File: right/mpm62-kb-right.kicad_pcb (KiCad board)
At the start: 2 copper layers, 161.9 x 95.2 mm, 72 parts, among them J1 Conn_01x04_Male, SW1 SW_Push, U1 MCP23018-E_SP

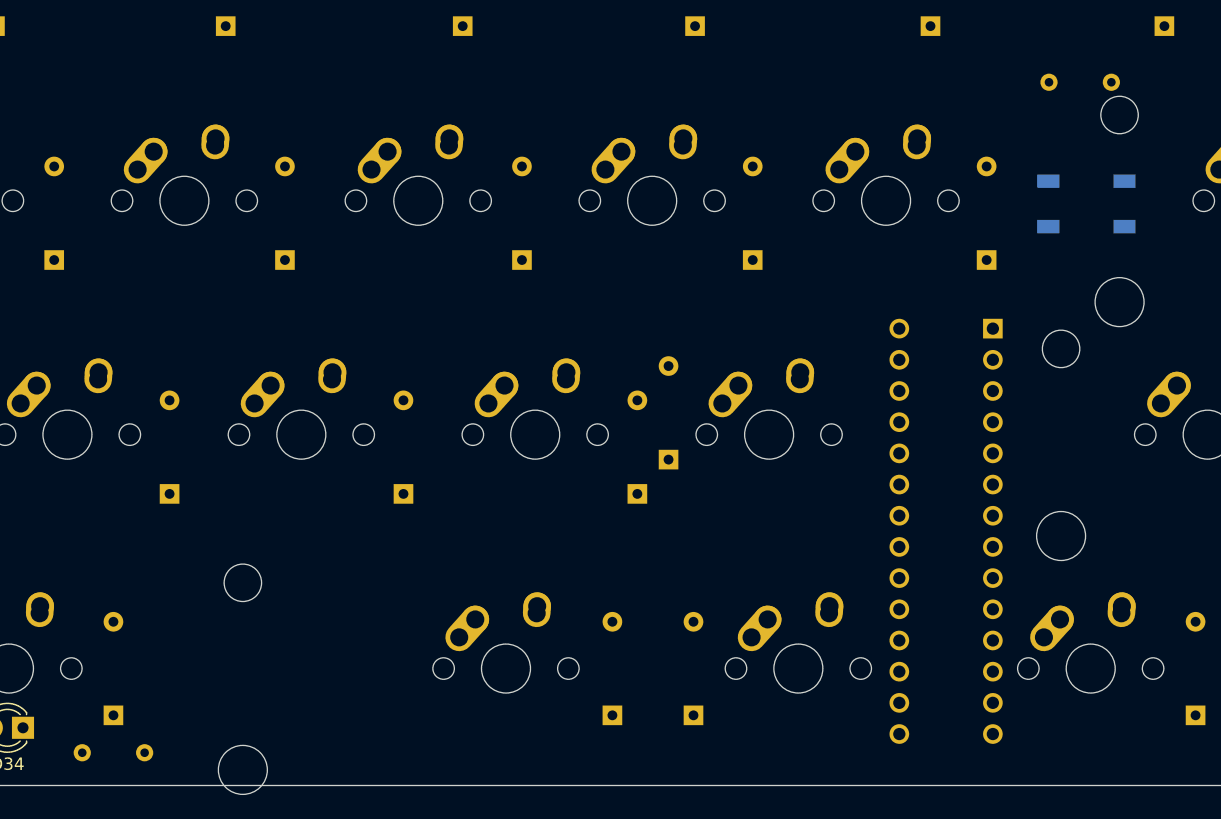
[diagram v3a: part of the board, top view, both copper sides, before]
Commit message: Fix resistor footprint, clean up layout.
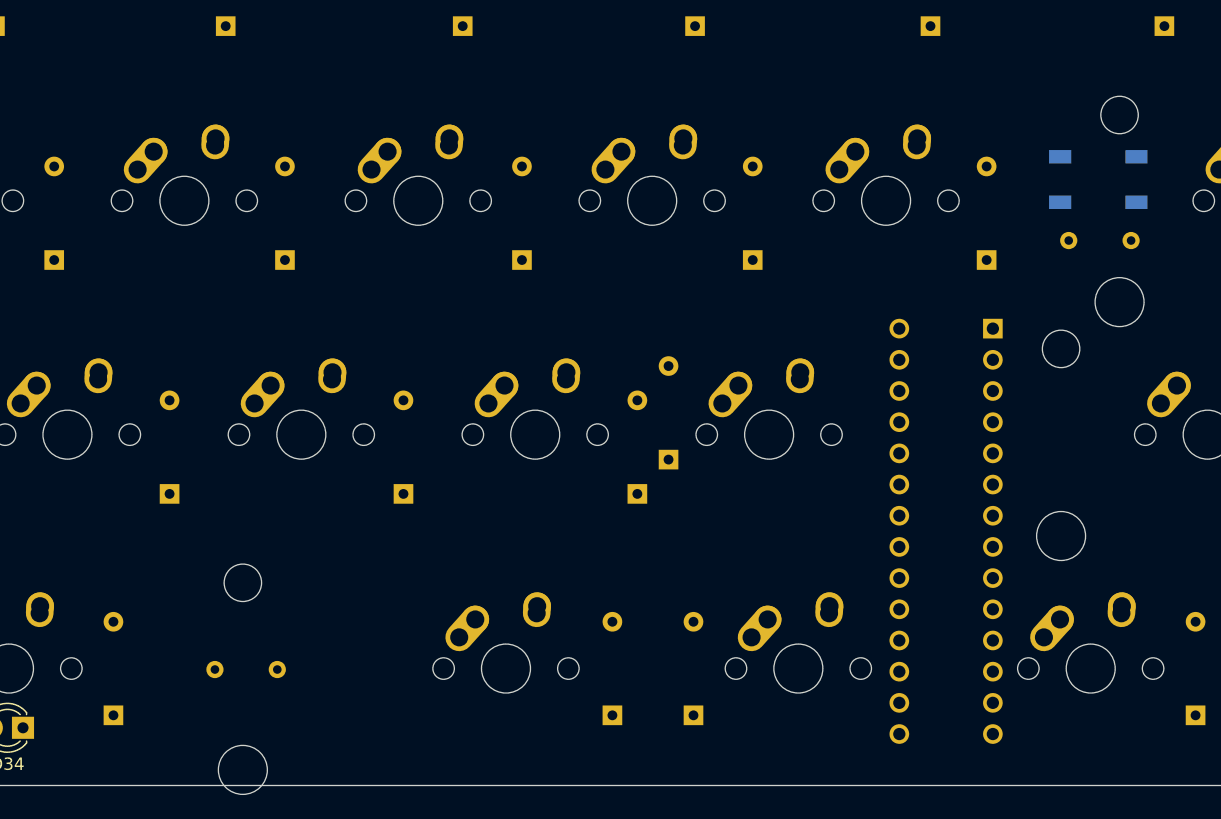
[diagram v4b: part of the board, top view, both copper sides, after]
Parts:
- R1, R2: footprint Resistor_THT:R_Axial_DIN0204_L3.6mm_D1.6mm_P5.08mm_Vertical -> Resistor_THT:R_Axial_DIN0204_L3.6mm_D1.6mm_P5.08mm_Horizontal
- moved R2 13.0 mm to (172.0, 98.5)
- moved R1 12.8 mm to (107.6, 133.4)
- moved SW1 2.21 mm to (174.4, 93.5), turned to 180 degrees
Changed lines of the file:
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@@
     (add_net VCC)
+  )
+  (module Resistor_THT:R_Axial_DIN0204_L3.6mm_D1.6mm_P5.08mm_Horizontal (layer B.Cu)
+    (at 172.04 98.49)
+    (descr "Resistor, Axial_DIN0204 series, Axial, Horizontal, pin pitch=5.08mm, 0.167W, length*diameter=3.6*1.6mm^2, http://cdn-reichelt.de/documents/datenblatt/B400/1_4W%23YAG.pdf")
+    (tags "Resistor Axial_DIN0204 series Axial Horizontal pin pitch 5.08mm 0.167W length 3.6mm diameter 1.6mm")
+    (fp_text reference R2 (at 2.54 1.92) (layer B.SilkS)
+      (effects (font (size 1 1) (thickness 0.15)) (justify mirror))
+    )
+    (fp_text value R_Small (at 2.54 -1.92) (layer B.Fab)
+      (effects (font (size 1 1) (thickness 0.15)) (justify mirror))
+    )
+    (fp_text user %R (at 2.54 0) (layer B.Fab)
+      (effects (font (size 0.72 0.72) (thickness 0.108)) (justify mirror))
+    )
+    (fp_line (start 6.03 1.05) (end -0.95 1.05) (layer B.CrtYd) (width 0.05))
+    (fp_line (start 6.03 -1.05) (end 6.03 1.05) (layer B.CrtYd) (width 0.05))
+    (fp_line (start -0.95 -1.05) (end 6.03 -1.05) (layer B.CrtYd) (width 0.05))
+    (fp_line (start -0.95 1.05) (end -0.95 -1.05) (layer B.CrtYd) (width 0.05))
+    (fp_line (start 0.62 -0.92) (end 4.46 -0.92) (layer B.SilkS) (width 0.12))
+    (fp_line (start 0.62 0.92) (end 4.46 0.92) (layer B.SilkS) (width 0.12))
+    (fp_line (start 5.08 0) (end 4.34 0) (layer B.Fab) (width 0.1))
+    (fp_line (start 0 0) (end 0.74 0) (layer B.Fab) (width 0.1))
+    (fp_line (start 4.34 0.8) (end 0.74 0.8) (layer B.Fab) (width 0.1))
+    (fp_line (start 4.34 -0.8) (end 4.34 0.8) (layer B.Fab) (width 0.1))
+    (fp_line (start 0.74 -0.8) (end 4.34 -0.8) (layer B.Fab) (width 0.1))
+    (fp_line (start 0.74 0.8) (end 0.74 -0.8) (layer B.Fab) (width 0.1))
+    (pad 2 thru_hole oval (at 5.08 0) (size 1.4 1.4) (drill 0.7) (layers *.Cu *.Mask)
+      (net 53 "Net-(R2-Pad2)"))
+    (pad 1 thru_hole circle (at 0 0) (size 1.4 1.4) (drill 0.7) (layers *.Cu *.Mask)
+      (net 41 VCC))
+    (model ${KISYS3DMOD}/Resistor_THT.3dshapes/R_Axial_DIN0204_L3.6mm_D1.6mm_P5.08mm_Horizontal.wrl
+      (at (xyz 0 0 0))
+      (scale (xyz 1 1 1))
+      (rotate (xyz 0 0 0))
+    )
+  )
+  (module Resistor_THT:R_Axial_DIN0204_L3.6mm_D1.6mm_P5.08mm_Horizontal (layer B.Cu)
+    (at 107.58 133.43 180)
+    (descr "Resistor, Axial_DIN0204 series, Axial, Horizontal, pin pitch=5.08mm, 0.167W, length*diameter=3.6*1.6mm^2, http://cdn-reichelt.de/documents/datenblatt/B400/1_4W%23YAG.pdf")
+    (tags "Resistor Axial_DIN0204 series Axial Horizontal pin pitch 5.08mm 0.167W length 3.6mm diameter 1.6mm")
+    (fp_text reference R1 (at 2.54 1.92) (layer B.SilkS)
+      (effects (font (size 1 1) (thickness 0.15)) (justify mirror))
+    )
+    (fp_text value R_Small (at 2.54 -1.92) (layer B.Fab)
+      (effects (font (size 1 1) (thickness 0.15)) (justify mirror))
+    )
+    (fp_text user %R (at 2.54 0) (layer B.Fab)
+      (effects (font (size 0.72 0.72) (thickness 0.108)) (justify mirror))
+    )
+    (fp_line (start 6.03 1.05) (end -0.95 1.05) (layer B.CrtYd) (width 0.05))
+    (fp_line (start 6.03 -1.05) (end 6.03 1.05) (layer B.CrtYd) (width 0.05))
+    (fp_line (start -0.95 -1.05) (end 6.03 -1.05) (layer B.CrtYd) (width 0.05))
+    (fp_line (start -0.95 1.05) (end -0.95 -1.05) (layer B.CrtYd) (width 0.05))
+    (fp_line (start 0.62 -0.92) (end 4.46 -0.92) (layer B.SilkS) (width 0.12))
+    (fp_line (start 0.62 0.92) (end 4.46 0.92) (layer B.SilkS) (width 0.12))
+    (fp_line (start 5.08 0) (end 4.34 0) (layer B.Fab) (width 0.1))
+    (fp_line (start 0 0) (end 0.74 0) (layer B.Fab) (width 0.1))
+    (fp_line (start 4.34 0.8) (end 0.74 0.8) (layer B.Fab) (width 0.1))
+    (fp_line (start 4.34 -0.8) (end 4.34 0.8) (layer B.Fab) (width 0.1))
+    (fp_line (start 0.74 -0.8) (end 4.34 -0.8) (layer B.Fab) (width 0.1))
+    (fp_line (start 0.74 0.8) (end 0.74 -0.8) (layer B.Fab) (width 0.1))
+    (pad 2 thru_hole oval (at 5.08 0 180) (size 1.4 1.4) (drill 0.7) (layers *.Cu *.Mask)
+      (net 40 "Net-(D34-Pad1)"))
+    (pad 1 thru_hole circle (at 0 0 180) (size 1.4 1.4) (drill 0.7) (layers *.Cu *.Mask)
+      (net 52 "Net-(R1-Pad1)"))
+    (model ${KISYS3DMOD}/Resistor_THT.3dshapes/R_Axial_DIN0204_L3.6mm_D1.6mm_P5.08mm_Horizontal.wrl
+      (at (xyz 0 0 0))
+      (scale (xyz 1 1 1))
+      (rotate (xyz 0 0 0))
+    )
   )
   (module MX_Alps_Hybrid:MX-3U-NoLED (layer F.Cu)
@@
     (pad 2 thru_hole oval (at 2.5 -4.5 86.0548) (size 2.831378 2.25) (drill 1.47 (offset 0.290689 0)) (layers *.Cu B.Mask)
       (net 17 "Net-(D11-Pad2)"))
-  )
-  (module Resistor_THT:R_Axial_DIN0204_L3.6mm_D1.6mm_P5.08mm_Vertical (layer B.Cu)
-    (at 170.434 85.598)
-    (descr "Resistor, Axial_DIN0204 series, Axial, Vertical, pin pitch=5.08mm, 0.167W, length*diameter=3.6*1.6mm^2, http://cdn-reichelt.de/documents/datenblatt/B400/1_4W%23YAG.pdf")
-    (tags "Resistor Axial_DIN0204 series Axial Vertical pin pitch 5.08mm 0.167W length 3.6mm diameter 1.6mm")
-    (fp_text reference R2 (at 2.54 1.92) (layer B.SilkS)
-      (effects (font (size 1 1) (thickness 0.15)) (justify mirror))
-    )
-    (fp_text value R_Small (at 2.54 -1.92) (layer B.Fab)
-      (effects (font (size 1 1) (thickness 0.15)) (justify mirror))
-    )
-    (fp_text user %R (at 2.54 1.92) (layer B.Fab)
-      (effects (font (size 1 1) (thickness 0.15)) (justify mirror))
-    )
-    (fp_line (start 6.03 1.05) (end -1.05 1.05) (layer B.CrtYd) (width 0.05))
-    (fp_line (start 6.03 -1.05) (end 6.03 1.05) (layer B.CrtYd) (width 0.05))
-    (fp_line (start -1.05 -1.05) (end 6.03 -1.05) (layer B.CrtYd) (width 0.05))
-    (fp_line (start -1.05 1.05) (end -1.05 -1.05) (layer B.CrtYd) (width 0.05))
-    (fp_line (start 0.92 0) (end 4.08 0) (layer B.SilkS) (width 0.12))
-    (fp_line (start 0 0) (end 5.08 0) (layer B.Fab) (width 0.1))
-    (fp_circle (center 0 0) (end 0.92 0) (layer B.SilkS) (width 0.12))
-    (fp_circle (center 0 0) (end 0.8 0) (layer B.Fab) (width 0.1))
-    (pad 2 thru_hole oval (at 5.08 0) (size 1.4 1.4) (drill 0.7) (layers *.Cu *.Mask)
-      (net 53 "Net-(R2-Pad2)"))
-    (pad 1 thru_hole circle (at 0 0) (size 1.4 1.4) (drill 0.7) (layers *.Cu *.Mask)
-      (net 41 VCC))
-    (model ${KISYS3DMOD}/Resistor_THT.3dshapes/R_Axial_DIN0204_L3.6mm_D1.6mm_P5.08mm_Vertical.wrl
-      (at (xyz 0 0 0))
-      (scale (xyz 1 1 1))
-      (rotate (xyz 0 0 0))
-    )
-  )
-  (module Resistor_THT:R_Axial_DIN0204_L3.6mm_D1.6mm_P5.08mm_Vertical (layer B.Cu)
-    (at 96.774 140.208 180)
-    (descr "Resistor, Axial_DIN0204 series, Axial, Vertical, pin pitch=5.08mm, 0.167W, length*diameter=3.6*1.6mm^2, http://cdn-reichelt.de/documents/datenblatt/B400/1_4W%23YAG.pdf")
-    (tags "Resistor Axial_DIN0204 series Axial Vertical pin pitch 5.08mm 0.167W length 3.6mm diameter 1.6mm")
-    (fp_text reference R1 (at 2.54 1.92) (layer B.SilkS)
-      (effects (font (size 1 1) (thickness 0.15)) (justify mirror))
-    )
-    (fp_text value R_Small (at 2.54 -1.92) (layer B.Fab)
-      (effects (font (size 1 1) (thickness 0.15)) (justify mirror))
-    )
-    (fp_text user %R (at 2.54 1.92) (layer B.Fab)
-      (effects (font (size 1 1) (thickness 0.15)) (justify mirror))
-    )
-    (fp_line (start 6.03 1.05) (end -1.05 1.05) (layer B.CrtYd) (width 0.05))
-    (fp_line (start 6.03 -1.05) (end 6.03 1.05) (layer B.CrtYd) (width 0.05))
-    (fp_line (start -1.05 -1.05) (end 6.03 -1.05) (layer B.CrtYd) (width 0.05))
-    (fp_line (start -1.05 1.05) (end -1.05 -1.05) (layer B.CrtYd) (width 0.05))
-    (fp_line (start 0.92 0) (end 4.08 0) (layer B.SilkS) (width 0.12))
-    (fp_line (start 0 0) (end 5.08 0) (layer B.Fab) (width 0.1))
-    (fp_circle (center 0 0) (end 0.92 0) (layer B.SilkS) (width 0.12))
-    (fp_circle (center 0 0) (end 0.8 0) (layer B.Fab) (width 0.1))
-    (pad 2 thru_hole oval (at 5.08 0 180) (size 1.4 1.4) (drill 0.7) (layers *.Cu *.Mask)
-      (net 40 "Net-(D34-Pad1)"))
-    (pad 1 thru_hole circle (at 0 0 180) (size 1.4 1.4) (drill 0.7) (layers *.Cu *.Mask)
-      (net 52 "Net-(R1-Pad1)"))
-    (model ${KISYS3DMOD}/Resistor_THT.3dshapes/R_Axial_DIN0204_L3.6mm_D1.6mm_P5.08mm_Vertical.wrl
-      (at (xyz 0 0 0))
-      (scale (xyz 1 1 1))
-      (rotate (xyz 0 0 0))
-    )
   )
   (module digikey-footprints:DIP-28_W7.62mm (layer B.Cu)
@@
   )
   (module random-keyboard-parts:SKQG-1155865 (layer B.Cu)
-    (at 173.482 95.504)
+    (at 174.45 93.52 180)
     (attr smd)
     (fp_text reference SW1 (at 0 -4.064) (layer B.SilkS)
@@
     (fp_line (start 2.6 -1.1) (end 1.1 -2.6) (layer B.Fab) (width 0.15))
     (fp_line (start -2.6 -1.1) (end -1.1 -2.6) (layer B.Fab) (width 0.15))
-    (pad 4 smd rect (at -3.1 -1.85) (size 1.8 1.1) (layers B.Cu B.Paste B.Mask))
-    (pad 3 smd rect (at 3.1 1.85) (size 1.8 1.1) (layers B.Cu B.Paste B.Mask))
-    (pad 2 smd rect (at -3.1 1.85) (size 1.8 1.1) (layers B.Cu B.Paste B.Mask)
+    (pad 4 smd rect (at -3.1 -1.85 180) (size 1.8 1.1) (layers B.Cu B.Paste B.Mask))
+    (pad 3 smd rect (at 3.1 1.85 180) (size 1.8 1.1) (layers B.Cu B.Paste B.Mask))
+    (pad 2 smd rect (at -3.1 1.85 180) (size 1.8 1.1) (layers B.Cu B.Paste B.Mask)
       (net 53 "Net-(R2-Pad2)"))
-    (pad 1 smd rect (at 3.1 -1.85) (size 1.8 1.1) (layers B.Cu B.Paste B.Mask)
+    (pad 1 smd rect (at 3.1 -1.85 180) (size 1.8 1.1) (layers B.Cu B.Paste B.Mask)
       (net 1 GND))
     (model ${KISYS3DMOD}/Button_Switch_SMD.3dshapes/SW_SPST_TL3342.step

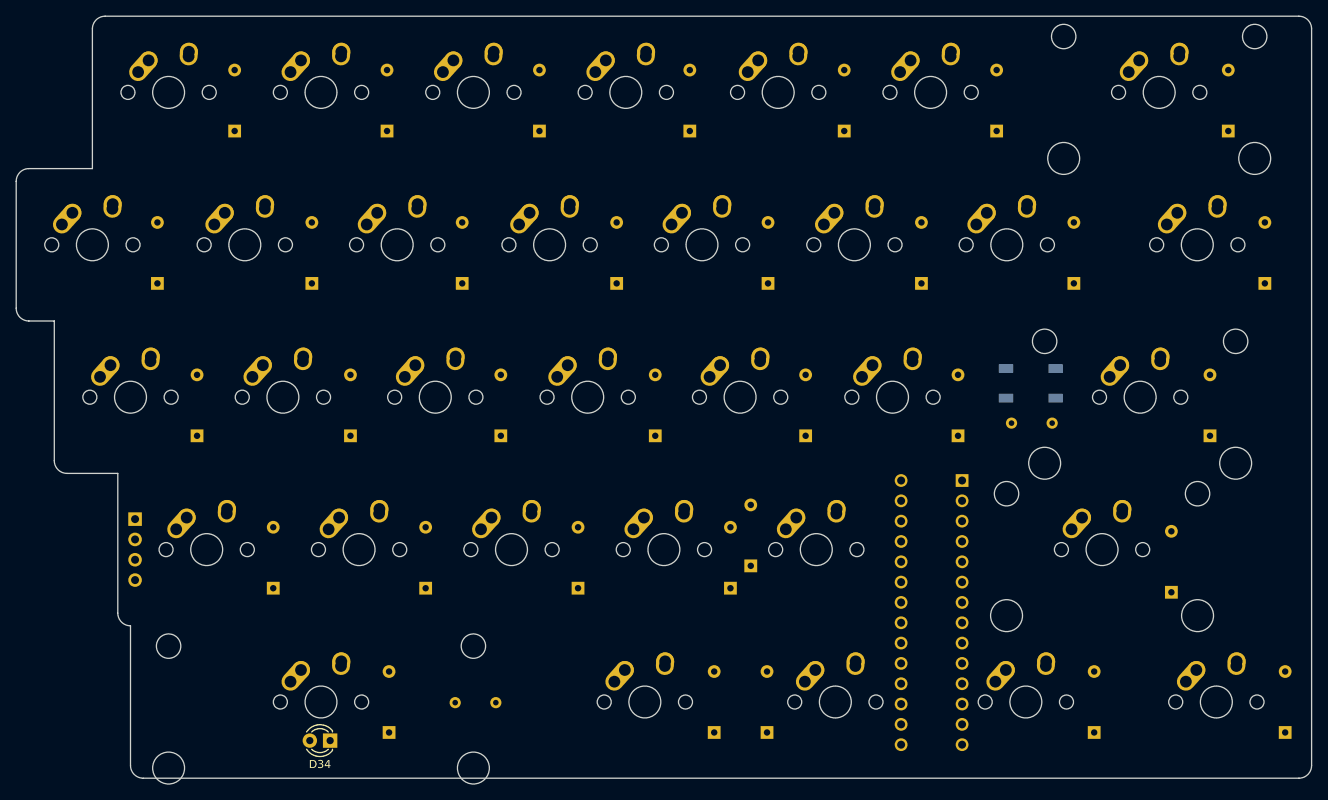
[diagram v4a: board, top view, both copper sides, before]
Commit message: Finished right side routing, some simplification, ground fill.
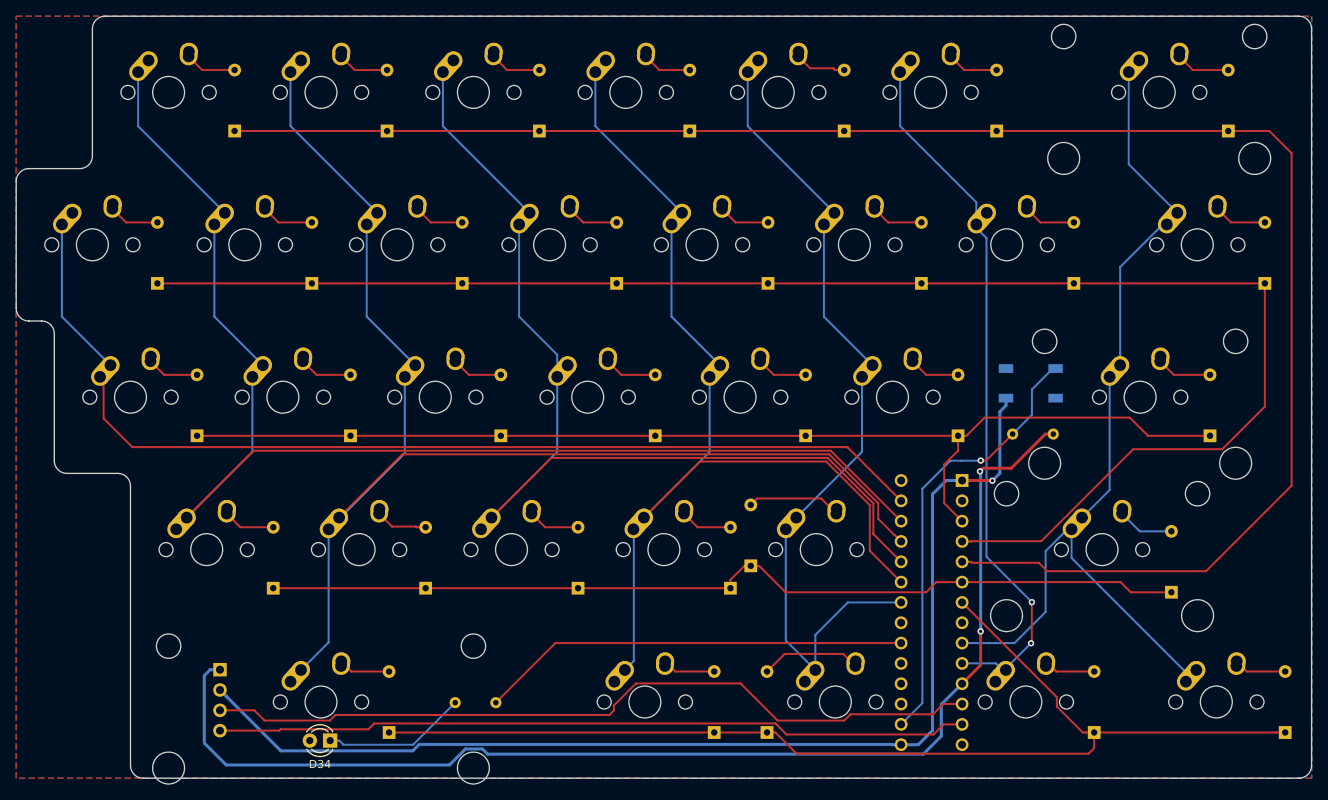
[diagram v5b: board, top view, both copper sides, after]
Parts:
- moved J1 21.6 mm to (73.1, 129.3)
- moved R2 5.40 mm to (177.3, 99.9), turned to 180 degrees
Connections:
- MX29 pad 1: Net-(MX29-Pad1) -> COL13
- MX30 pad 1: Net-(MX29-Pad1) -> COL13
- MX31 pad 1: Net-(MX29-Pad1) -> COL13
- MX32 pad 1: Net-(MX29-Pad1) -> COL13
- MX33 pad 1: Net-(MX29-Pad1) -> COL13
- U1 pad 3: ROW0 -> ROW2
- U1 pad 5: ROW2 -> ROW0
- U1 pad 9: (no net) -> COL13
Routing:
- net ROW0: track 0.00 -> 220.9 mm
- net ROW1: track 0.00 -> 198.7 mm
- net COL8: track 0.00 -> 163.4 mm
- net COL7: track 0.00 -> 161.6 mm
- net VCC: track 0.00 -> 152.2 mm, vias 0 -> 2
- net GND: track 0.00 -> 142.1 mm, vias 0 -> 1
- net ROW2: track 0.00 -> 140.8 mm
- net ROW4: track 0.00 -> 139.3 mm
- net COL6: track 0.00 -> 130.5 mm
- net COL9: track 0.00 -> 130.0 mm
- net COL10: track 0.00 -> 125.9 mm
- net ROW3: track 0.00 -> 116.5 mm
- net COL13: track 0.00 -> 108.4 mm
- net COL11: track 0.00 -> 99.1 mm
- net Net-(J1-Pad3): track 0.00 -> 98.4 mm
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- added copper zone on B.Cu, net GND
- added copper zone on F.Cu, net GND
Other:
- outline, holes or cut-outs redrawn

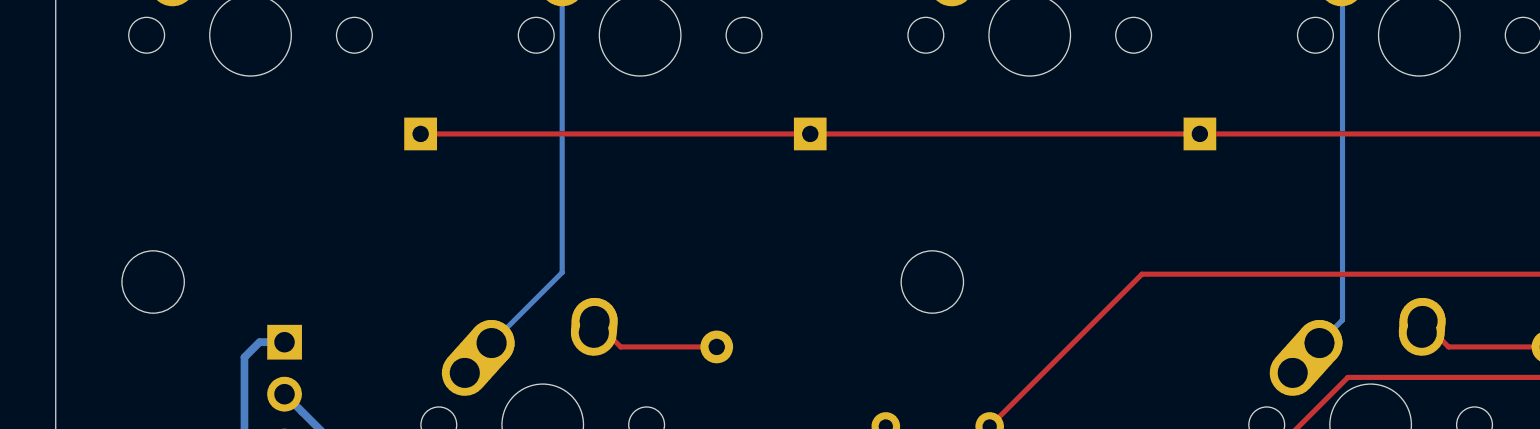
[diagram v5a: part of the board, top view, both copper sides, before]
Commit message: Add version text to front silk layer
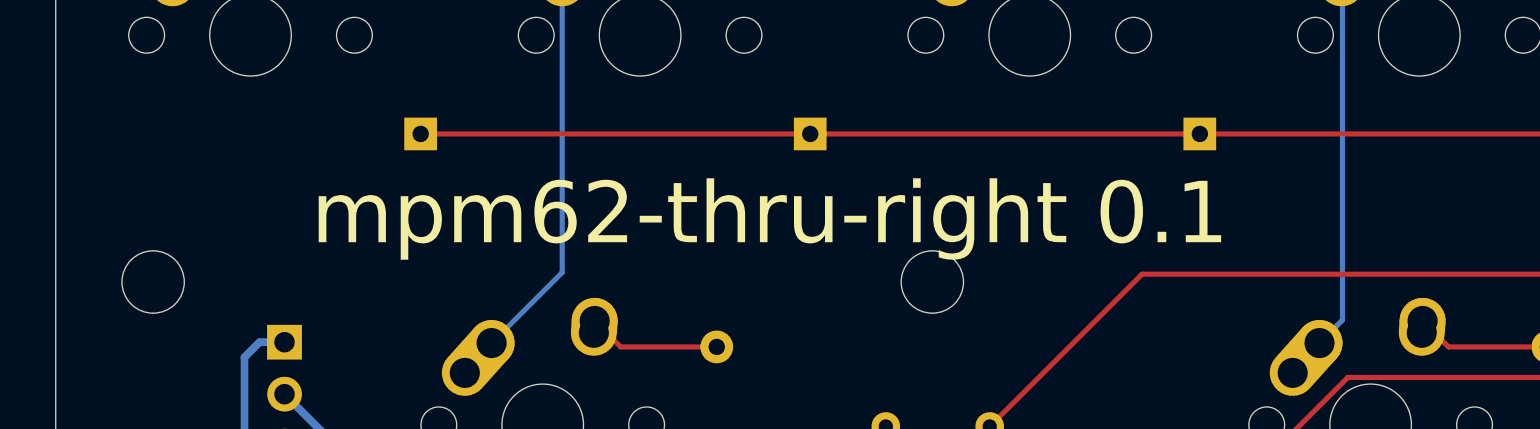
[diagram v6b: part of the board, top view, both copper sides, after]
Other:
- board text added: "mpm62-thru-right 0.1"
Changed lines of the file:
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@@
   (general
     (thickness 1.6)
-    (drawings 20)
+    (drawings 21)
     (tracks 342)
     (zones 0)
@@
       (net 2 "Net-(D1-Pad2)"))
   )
+  (gr_text "mpm62-thru-right 0.1" (at 96.8375 123.03125) (layer F.SilkS)
+    (effects (font (size 3 3) (thickness 0.15)))
+  )
   (gr_line (start 57.15 65.0875) (end 57.15 49.2125) (layer Edge.Cuts) (width 0.05))
